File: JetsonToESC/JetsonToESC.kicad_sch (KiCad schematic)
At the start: 0 parts

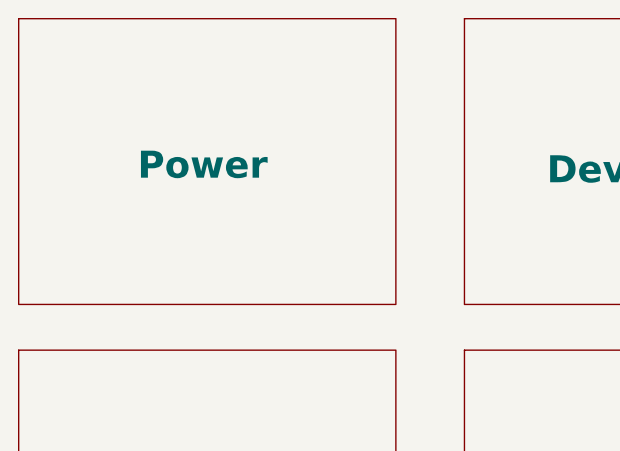
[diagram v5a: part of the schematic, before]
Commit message: Edit around current sensor
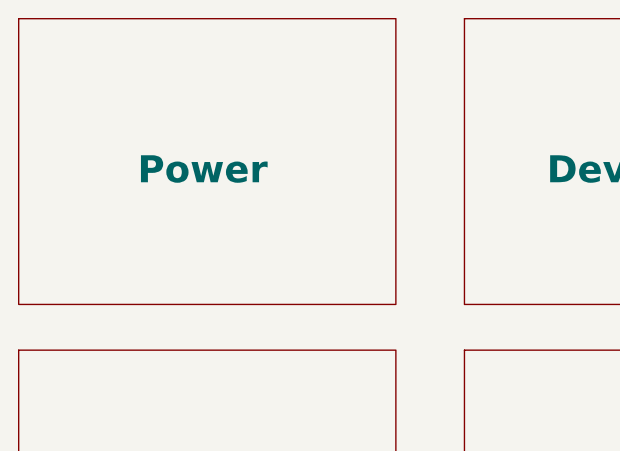
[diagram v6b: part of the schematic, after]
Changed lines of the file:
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@@
 		)
 		(property "Sheetname" "Power"
-			(at 70.358 44.704 0)
+			(at 70.358 45.212 0)
 			(effects
 				(font
